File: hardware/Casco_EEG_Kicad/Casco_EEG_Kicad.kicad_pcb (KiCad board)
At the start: 2 copper layers, 116 x 64.5 mm, 101 parts, among them J1 Jack_Touch-Proof, J10 Jack_Touch-Proof, J11 FTSH-105-XX-X-DV, J12 USB_B_Micro, J2 Jack_Touch-Proof, J3 Jack_Touch-Proof, J4 Jack_Touch-Proof, J5 Jack_Touch-Proof, J6 Jack_Touch-Proof, J7 Jack_Touch-Proof, J8 Jack_Touch-Proof, J9 Jack_Touch-Proof, Q1 FS8205A, SW6 SW_Push, U1 ADS1299, U2 HC-05, U3 LPC845M301JBD48E, U4 TP4056-42-ESOP8, U5 DW01A, U6 AMS1117-3.3

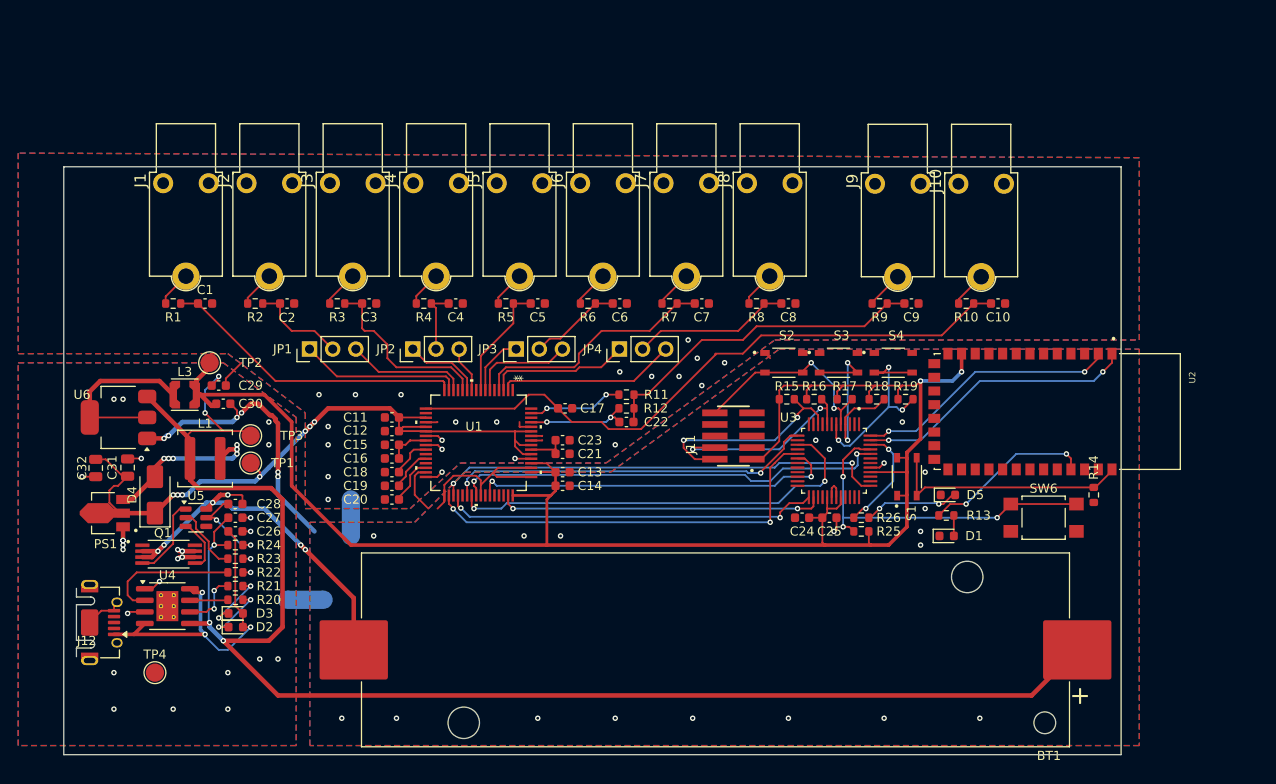
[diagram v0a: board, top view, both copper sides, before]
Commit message: Nuevos cambios al PCB, mejoro planos, regulo 3,3V desde 5V, etc
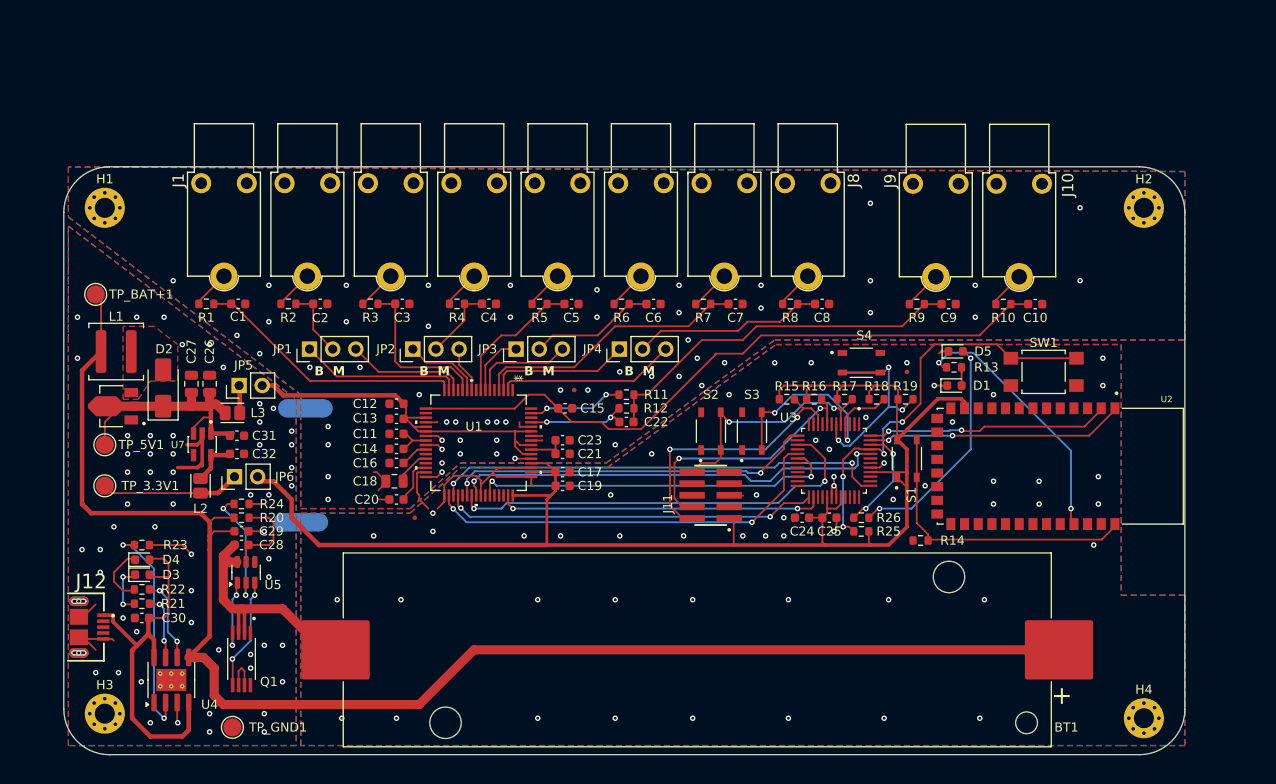
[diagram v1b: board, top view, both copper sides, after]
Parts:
- removed the C26 at (94.8, 116.5)
- removed the C27 at (94.8, 115.0)
- removed the R23 at (94.8, 119.5)
- removed U6: AMS1117-3.3, Package_TO_SOT_SMD:SOT-223-3_TabPin2
- added C29: 10u, Capacitor_SMD:C_0603_1608Metric, F.Cu at (95.5, 116.5)
- added C30: 0.1u, Capacitor_SMD:C_0603_1608Metric, F.Cu at (84.6, 126.0)
- added FID1: Fiducial, Fiducial:Fiducial_0.5mm_Mask1mm, F.Cu at (114.5, 115.0)
- added FID2: Fiducial, Fiducial:Fiducial_0.5mm_Mask1mm, F.Cu at (132.0, 101.0)
- added FID3: Fiducial, Fiducial:Fiducial_0.5mm_Mask1mm, F.Cu at (168.5, 99.0)
- added H1: MountingHole, MountingHole:MountingHole_2.2mm_M2_Pad_Via, F.Cu at (80.5, 81.0)
- added H2: MountingHole, MountingHole:MountingHole_2.2mm_M2_Pad_Via, F.Cu at (194.5, 81.0)
- added H3: MountingHole, MountingHole:MountingHole_2.2mm_M2_Pad_Via, F.Cu at (80.5, 136.5)
- added H4: MountingHole, MountingHole:MountingHole_2.2mm_M2_Pad_Via, F.Cu at (194.5, 137.0)
- added JP5: Jumper_2_Open, Connector_PinHeader_2.54mm:PinHeader_1x02_P2.54mm_Vertical, F.Cu at (95.2, 100.5)
- added JP6: Jumper_2_Open, Connector_PinHeader_2.54mm:PinHeader_1x02_P2.54mm_Vertical, F.Cu at (94.7, 110.5)
- added L3: HZ0805E601R-10, Inductor_SMD:L_Eaton_MCL2012V1, F.Cu at (94.5, 103.5)
- added R20: 100, Resistor_SMD:R_0603_1608Metric, F.Cu at (95.5, 115.0)
- added U7: AP2112K-3.3TRG1, Huellas:SOT95P285X140-5N, F.Cu at (91.2, 107.0)
- C18: renamed from C19; footprint Capacitor_SMD:C_0603_1608Metric -> Capacitor_SMD:C_0805_2012Metric
- C26: renamed from C31; value 12u -> 10u
- C27: renamed from C32; value 12u -> 10u
- J12: value USB_B_Micro -> USB3080-XX-00-A_REVE; footprint Connector_USB:USB_Micro-AB_Molex_47590-0001 -> Huellas:GCT_USB3080-XX-00-A_REVE
- L2: renamed from L3; value L -> HZ0805E601R-10; footprint Inductor_SMD:L_Coilcraft_LPS3010 -> Inductor_SMD:L_Eaton_MCL2012V1
- PS1: value ME2108A33P -> ME2108A50P
- R11: value R -> 0
- R13: value R -> 2.2k
- R14: value R -> 10k
- R24: value 100 -> 1k
- moved TP_BAT+1 23.0 mm to (79.5, 90.5)
- moved NT1 21.0 mm to (102.5, 103.0)
- moved R14 19.6 mm to (170.0, 117.5), turned to 180 degrees
- moved TP_3.3V1 17.7 mm to (80.5, 111.5)
- moved D1 16.5 mm to (173.7, 100.5)
- moved R13 16.3 mm to (173.7, 98.5)
- moved TP_5V1 16.1 mm to (80.5, 107.0)
- moved SW1 16.0 mm to (183.5, 99.0)
- moved D5 15.8 mm to (173.8, 96.8)
- moved L1 15.3 mm to (81.7, 96.8)
- moved Q1 14.0 mm to (95.5, 130.5), turned to -90 degrees
- moved C27 14.0 mm to (90.0, 100.3), turned to 90 degrees
- moved C26 12.9 mm to (92.0, 100.3)
- moved S3 12.1 mm to (151.5, 105.5), turned to 90 degrees
- moved D4 11.8 mm to (84.6, 119.6)
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- renumbered C15 to C11, C11 to C12, C12 to C13, C16 to C14, C17 to C15, C18 to C16, C13 to C17, C14 to C19, C29 to C31, C30 to C32, D4 to D2, D2 to D3, D3 to D4, NT2 to NT1, NT1 to NT2, R20 to R21, R21 to R22, R22 to R23, SW6 to SW1, TP2 to TP_3.3V1, TP1 to TP_5V1, TP3 to TP_BAT+1, TP4 to TP_GND1
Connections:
- C26 pad 1: +5V -> /Alimentacion/5V_reg
- C27 pad 1: +5V -> /Alimentacion/5V_reg
- C31 pad 1: /Alimentacion/VOUT+ -> /Alimentacion/5V_reg
- C31 pad 2: GNDA -> GNDPWR
- C32 pad 1: +3.3V -> Net-(U7-VOUT)
- C32 pad 2: GNDD -> GNDPWR
- D2 pad 1: +5V -> /Alimentacion/5V_reg
- L2 pad 1: Net-(U6-VO) -> Net-(U7-VOUT)
- L2 pad 2: +3.3V -> Net-(JP6-A)
- NT1 pad 2: GNDD -> GNDA
- NT2 pad 1: GNDA -> GNDPWR
- PS1 pad 2: +5V -> /Alimentacion/5V_reg
- R24 pad 1: /Alimentacion/VOUT+ -> Net-(U5-CS)
- R24 pad 2: Net-(U5-VCC) -> GNDPWR
- TP_3.3V1 pad 1: +3.3V -> Net-(JP6-A)
- TP_5V1 pad 1: +5V -> /Alimentacion/5V_reg
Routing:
- net +5V: track 77.9 -> 41.7 mm, vias 7 -> 0
- net /Alimentacion/5V_reg: track 0.00 -> 28.5 mm
- net GNDD: track 64.6 -> 37.0 mm, vias 26 -> 55
- net +3.3V: track 187.6 -> 160.9 mm, vias 2 -> 0
- net Net-(D2-A): track 20.4 -> 0.00 mm, vias 6 -> 0
- net Net-(U6-VO): track 19.4 -> 0.00 mm
- net Net-(D5-A): track 10.6 -> 25.9 mm
- net Net-(JP6-A): track 0.00 -> 15.3 mm
- net /Alimentacion/V_BAT_N: track 46.5 -> 33.3 mm, vias 6 -> 0
- net /Alimentacion/VOUT+: track 176.7 -> 164.5 mm, vias 5 -> 0
- net GNDPWR: track 21.1 -> 32.6 mm, vias 27 -> 56
- net Net-(U2-PIO[8]): track 18.7 -> 28.7 mm
- net Net-(U4-PROG): track 15.0 -> 24.4 mm, vias 0 -> 2
- net /CPU/User_Button: track 38.5 -> 45.3 mm, vias 3 -> 4
- net /CPU/PIO0_03: track 22.1 -> 28.4 mm
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- added copper zone on F.Cu, net Net-(D2-A)
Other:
- board size 116 x 64.5 mm -> 123 x 64.5 mm
- board text added: "B M"

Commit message: Implemento pines I/O para trigger
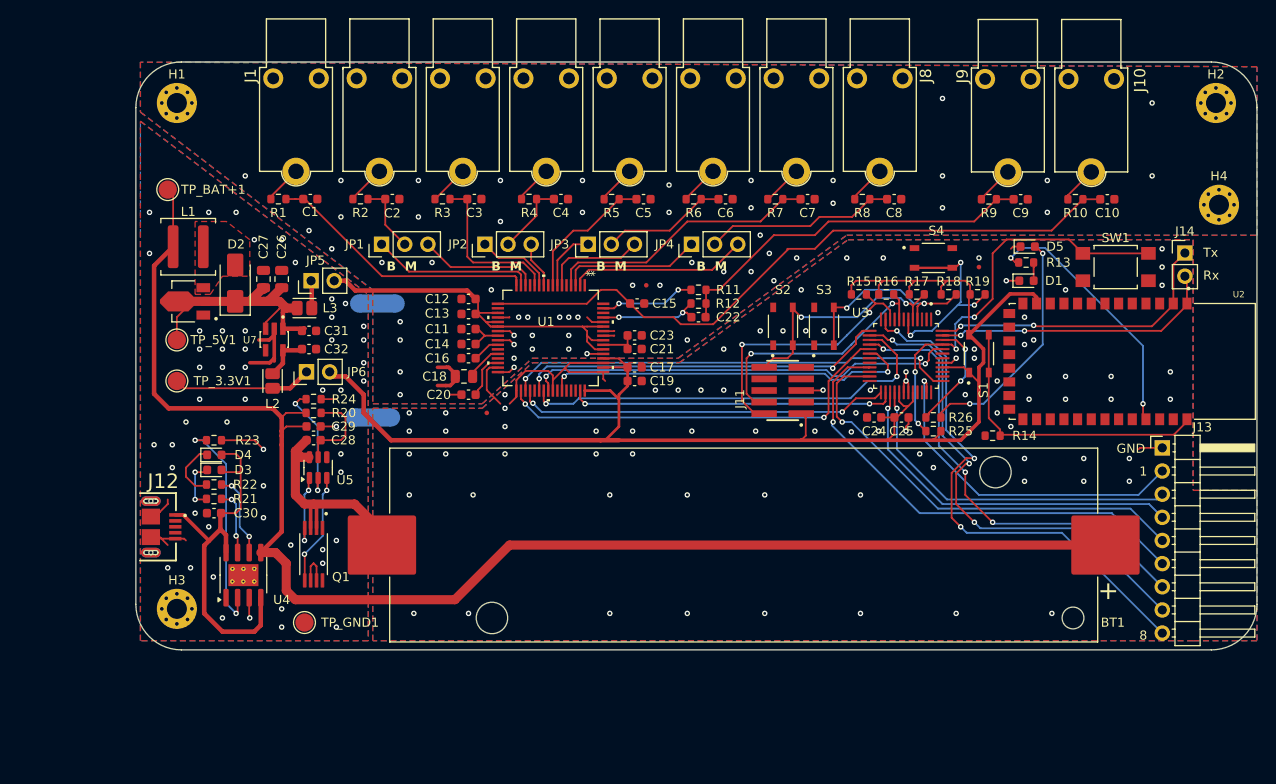
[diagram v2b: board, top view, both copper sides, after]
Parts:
- added J13: Conn_01x09_Pin, Connector_PinHeader_2.54mm:PinHeader_1x09_P2.54mm_Horizontal, F.Cu at (196.5, 107.3)
- added J14: Conn_01x02, Connector_PinHeader_2.54mm:PinHeader_1x02_P2.54mm_Vertical, F.Cu at (199.0, 86.0)
- moved H4 56.9 mm to (202.7, 80.7)
- moved U4 14.0 mm to (95.7, 121.3)
- moved C1 14.0 mm to (103.0, 80.0)
- moved C10 14.0 mm to (190.5, 80.1)
- moved C11 14.0 mm to (120.4, 94.3)
- moved C12 14.0 mm to (120.4, 91.0)
- moved C13 14.0 mm to (120.4, 92.7)
- moved C14 14.0 mm to (120.4, 96.0)
- moved C15 14.0 mm to (138.9, 91.5)
- moved C16 14.0 mm to (120.4, 97.5)
- moved C17 14.0 mm to (138.6, 98.5)
- moved C19 14.0 mm to (138.6, 100.0)
- moved C2 14.0 mm to (112.0, 80.0)
- moved C20 14.0 mm to (120.4, 101.5)
- moved C21 14.0 mm to (138.6, 96.5)
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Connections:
- U3 pad 11: unconnected-(U3-PIO1_0/CAPT_X1-Pad11) -> Net-(J13-Pin_9)
- U3 pad 14: unconnected-(U3-PIO1_1/CAPT_X2-Pad14) -> Net-(J13-Pin_8)
- U3 pad 16: unconnected-(U3-PIO1_2/CAPT_X3_-Pad16) -> Net-(J13-Pin_7)
- U3 pad 21: unconnected-(U3-PIO1_3/CAPT_X4-Pad21) -> Net-(J13-Pin_6)
- U3 pad 23: unconnected-(U3-PIO1_4/CAPT_X5-Pad23) -> Net-(J13-Pin_5)
- U3 pad 27: unconnected-(U3-PIO1_5/CAPT_X6-Pad27) -> Net-(J13-Pin_4)
- U3 pad 28: unconnected-(U3-PIO1_6/CAPT_X7-Pad28) -> Net-(J13-Pin_3)
- U3 pad 35: unconnected-(U3-PIO1_7/CAPT_X8-Pad35) -> Net-(J13-Pin_2)
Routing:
- net Net-(J13-Pin_9): track 0.00 -> 57.8 mm, vias 0 -> 3
- net Net-(J13-Pin_8): track 0.00 -> 54.5 mm, vias 0 -> 3
- net Net-(J13-Pin_6): track 0.00 -> 52.5 mm, vias 0 -> 1
- net Net-(J13-Pin_7): track 0.00 -> 50.1 mm, vias 0 -> 3
- net Net-(J13-Pin_5): track 0.00 -> 48.9 mm, vias 0 -> 1
- net Net-(J13-Pin_4): track 0.00 -> 39.6 mm, vias 0 -> 1
- net Net-(J13-Pin_3): track 0.00 -> 38.0 mm, vias 0 -> 1
- net Net-(J13-Pin_2): track 0.00 -> 37.5 mm, vias 0 -> 1
- net /CPU/TX_Master: track 26.7 -> 32.8 mm
- net /Alimentacion/V_BAT_N: track 33.3 -> 28.6 mm
- net GNDD: track 37.0 -> 41.3 mm, vias 55 -> 84
- net /CPU/PIO0_12: track 26.1 -> 22.0 mm
- net /CPU/RX_Master: track 28.9 -> 32.0 mm
- net GNDA: track 17.6 -> 20.2 mm
- net /Alimentacion/5V_reg: track 28.5 -> 30.9 mm
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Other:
- board text added: "1"
- board text added: "8"
- board text added: "GND"
- board text added: "Rx"
- board text added: "Tx"

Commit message: Actualizacion del modelo, agrego mini slide switch, agrego jumpers para comunicacion con modulo BT
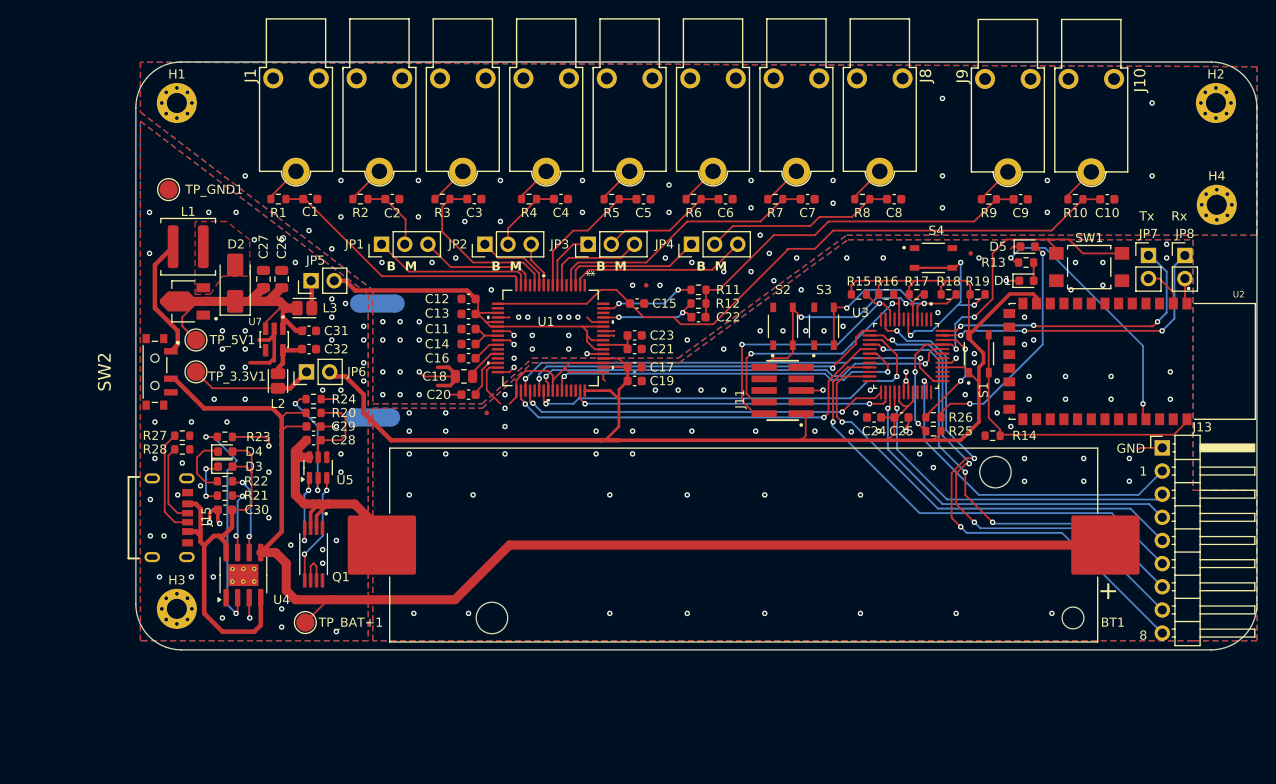
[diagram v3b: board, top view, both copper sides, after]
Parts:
- removed J12: USB3080-XX-00-A_REVE, Huellas:GCT_USB3080-XX-00-A_REVE
- removed J14: Conn_01x02, Connector_PinHeader_2.54mm:PinHeader_1x02_P2.54mm_Vertical
- added J15: USB4125-GF-A_REVA2, Huellas:GCT_USB4125-GF-A_REVA2, F.Cu at (86.5, 115.0)
- added JP7: Jumper_2_Open, Connector_PinHeader_2.54mm:PinHeader_1x02_P2.54mm_Vertical, F.Cu at (195.0, 86.2)
- added JP8: Jumper_2_Open, Connector_PinHeader_2.54mm:PinHeader_1x02_P2.54mm_Vertical, F.Cu at (199.0, 86.2)
- added R27: 5.1k, Resistor_SMD:R_0603_1608Metric, F.Cu at (89.0, 106.0)
- added R28: 5.1k, Resistor_SMD:R_0603_1608Metric, F.Cu at (89.0, 107.5)
- added SW2: PCM12SMTR, Huellas:SW_PCM12SMTR, F.Cu at (86.0, 99.0)
- moved TP_BAT+1 49.8 mm to (102.5, 126.5)
- moved TP_GND1 49.8 mm to (87.5, 79.0)
- moved SW1 2.91 mm to (188.5, 87.5)
- moved TP_3.3V1 2.32 mm to (90.5, 99.0)
- moved TP_5V1 2.09 mm to (90.5, 95.5)
- moved FID3 1.75 mm to (175.5, 86.0)
- moved D3 1.25 mm to (93.7, 109.4)
- moved D4 1.25 mm to (93.7, 107.7)
- moved C30 1.25 mm to (93.7, 114.1)
- moved R21 1.25 mm to (93.7, 112.6)
- moved R22 1.25 mm to (93.7, 111.0)
- moved R23 1.25 mm to (93.7, 106.1)
- moved L2 0.59 mm to (99.5, 100.0)
- moved H4 0.24 mm to (202.5, 80.7)
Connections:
- L1 pad 1: /Alimentacion/VOUT+ -> Net-(L1-Pad1)
- U2 pad 1: /CPU/RX_Master -> Net-(JP8-B)
- U2 pad 2: /CPU/TX_Master -> Net-(JP7-B)
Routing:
- net /Alimentacion/VOUT+: track 164.2 -> 141.4 mm
- net Net-(L1-Pad1): track 0.00 -> 15.4 mm
- net Net-(J15-CC2): track 0.00 -> 11.2 mm
- net Net-(J15-CC1): track 0.00 -> 8.22 mm
- net GNDPWR: track 32.0 -> 27.1 mm, vias 53 -> 55
- net Net-(JP7-B): track 0.00 -> 4.72 mm
- net GNDA: track 20.2 -> 24.4 mm, vias 55 -> 66
- net /Alimentacion/V_BUSP: track 41.7 -> 45.6 mm
- net Net-(JP8-B): track 0.00 -> 3.01 mm
- net /CPU/RX_Master: track 32.0 -> 34.0 mm, vias 2 -> 3
- net Net-(JP6-A): track 15.3 -> 13.6 mm
- net /Alimentacion/5V_reg: track 30.9 -> 32.5 mm
- net /Adquisicion/E3: track 17.6 -> 19.1 mm
- net /Alimentacion/V_BAT_N: track 28.6 -> 29.7 mm
- net Net-(U4-PROG): track 24.4 -> 25.1 mm
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
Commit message: Modifico pistas, cambios menores
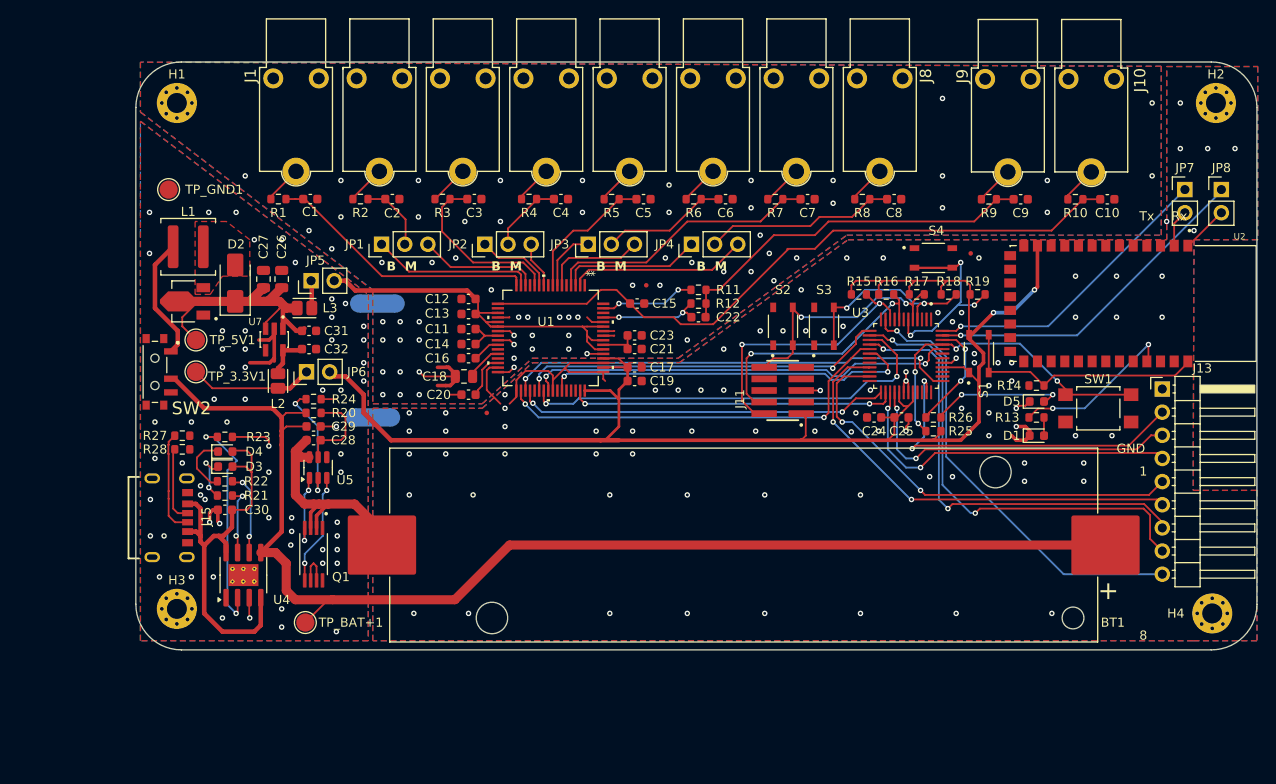
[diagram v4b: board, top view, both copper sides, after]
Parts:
- moved H4 44.8 mm to (202.0, 125.5)
- moved D1 17.0 mm to (182.8, 106.0)
- moved R13 17.0 mm to (182.7, 104.0)
- moved D5 17.0 mm to (182.8, 102.2)
- moved SW1 15.5 mm to (189.5, 103.0)
- moved JP7 8.26 mm to (199.0, 79.0)
- moved JP8 8.26 mm to (203.0, 79.0)
- moved R14 7.31 mm to (182.7, 100.5)
- moved J13 6.46 mm to (196.5, 100.9)
- moved U2 6.35 mm to (193.0, 91.5)
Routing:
- net Net-(D5-A): track 25.7 -> 14.7 mm
- net Net-(U2-PIO[8]): track 28.7 -> 18.5 mm
- net Net-(J13-Pin_9): track 57.8 -> 49.0 mm, vias 3 -> 1
- net /CPU/User_Button: track 45.0 -> 36.1 mm
- net Net-(U2-PIO[11]): track 33.0 -> 27.8 mm
- net +3.3V: track 162.0 -> 165.8 mm, vias 0 -> 2
- net /CPU/RX_Master: track 34.0 -> 37.8 mm, vias 3 -> 1
- net Net-(J13-Pin_6): track 52.5 -> 49.3 mm, vias 1 -> 2
- net Net-(J13-Pin_8): track 54.5 -> 52.0 mm, vias 3 -> 2
- net Net-(JP8-B): track 3.01 -> 5.17 mm
- net Net-(J13-Pin_5): track 48.9 -> 47.5 mm, vias 1 -> 2
- net Net-(J13-Pin_4): track 39.6 -> 38.2 mm, vias 1 -> 2
- net Net-(J13-Pin_3): track 38.0 -> 36.9 mm, vias 1 -> 2
- net Net-(J13-Pin_2): track 37.5 -> 38.4 mm, vias 1 -> 2
- net GNDD: track 41.3 -> 42.1 mm, vias 87 -> 88
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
